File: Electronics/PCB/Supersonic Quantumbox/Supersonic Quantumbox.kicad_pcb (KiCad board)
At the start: 2 copper layers, 15 parts, among them J1 USB_C_Receptacle_USB2.0, U1 Input_jack, U2 TL071, U3 PCM1808PWR, U4 AZ1117-5.0, U5 ESP32-S2-WROVER-I, U6 AZ1117-3.3, U7 PCM5100, U8 Output_jack

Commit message: Start work on PCB
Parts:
- added C1: 100n, Capacitor_SMD:C_0805_2012Metric_Pad1.18x1.45mm_HandSolder, F.Cu at (132.0, 146.0)
- added C10: 10uF, Capacitor_SMD:C_1206_3216Metric, F.Cu at (257.1, 70.5)
- added C11: 100n, Capacitor_SMD:C_0805_2012Metric_Pad1.18x1.45mm_HandSolder, F.Cu at (265.0, 131.0)
- added C12: 100n, Capacitor_SMD:C_0805_2012Metric_Pad1.18x1.45mm_HandSolder, F.Cu at (176.0, 71.0)
- added C13: 100n, Capacitor_SMD:C_0805_2012Metric_Pad1.18x1.45mm_HandSolder, F.Cu at (146.0, 59.0)
- added C14: 100n, Capacitor_SMD:C_0805_2012Metric_Pad1.18x1.45mm_HandSolder, F.Cu at (250.9, 131.0)
- added C15: 2.2uF, Capacitor_SMD:C_1206_3216Metric, F.Cu at (246.0, 139.0)
- added C16: 2.2uF, Capacitor_SMD:C_1206_3216Metric, F.Cu at (248.0, 144.0)
- added C17: 100n, Capacitor_SMD:C_0805_2012Metric_Pad1.18x1.45mm_HandSolder, F.Cu at (257.9, 131.0)
- added C18: 10uF, Capacitor_SMD:C_1206_3216Metric, F.Cu at (266.0, 141.0)
- added C19: 2.2n, Capacitor_SMD:C_0805_2012Metric_Pad1.18x1.45mm_HandSolder, F.Cu at (257.0, 154.0)
- added C2: 10uF, Capacitor_SMD:C_1206_3216Metric, F.Cu at (124.0, 142.0)
- added C20: 100n, Capacitor_SMD:C_0805_2012Metric_Pad1.18x1.45mm_HandSolder, F.Cu at (141.0, 131.0)
- added C21: 10uF, Capacitor_SMD:C_1206_3216Metric, F.Cu at (191.0, 150.0)
- added C3: 10uF, Capacitor_SMD:C_1206_3216Metric, F.Cu at (144.0, 140.0)
- added C4: 100n, Capacitor_SMD:C_0805_2012Metric_Pad1.18x1.45mm_HandSolder, F.Cu at (187.0, 146.0)
- added C5: 100n, Capacitor_SMD:C_0805_2012Metric_Pad1.18x1.45mm_HandSolder, F.Cu at (199.0, 142.0)
- added C6: 100n, Capacitor_SMD:C_0805_2012Metric_Pad1.18x1.45mm_HandSolder, F.Cu at (195.0, 147.0)
- added C7: 10uF, Capacitor_SMD:C_1206_3216Metric, F.Cu at (221.8, 69.0)
- added C8: 10uF, Capacitor_SMD:C_1206_3216Metric, F.Cu at (257.1, 51.5)
- added C9: 10uF, Capacitor_SMD:C_1206_3216Metric, F.Cu at (222.3, 50.0)
- added J2: Barrel_Jack_Switch, Connector_BarrelJack:BarrelJack_Horizontal, F.Cu at (204.0, 99.0)
- added O1: 128x64_OLED, SupersonicQuantumbox:128x64OLED, F.Cu at (70.0, 94.0)
- added R1: 2M2, Resistor_SMD:R_0805_2012Metric_Pad1.20x1.40mm_HandSolder, F.Cu at (137.0, 146.0)
- added R10: 470, Resistor_SMD:R_0805_2012Metric_Pad1.20x1.40mm_HandSolder, F.Cu at (255.0, 148.0)
- added R11: 5.1K, Resistor_SMD:R_0805_2012Metric_Pad1.20x1.40mm_HandSolder, F.Cu at (255.0, 107.0)
- added R12: 5.1K, Resistor_SMD:R_0805_2012Metric_Pad1.20x1.40mm_HandSolder, F.Cu at (248.0, 106.0)
- added R2: 2M2, Resistor_SMD:R_0805_2012Metric_Pad1.20x1.40mm_HandSolder, F.Cu at (142.0, 146.0)
- added R3: 100K, Resistor_SMD:R_0805_2012Metric_Pad1.20x1.40mm_HandSolder, F.Cu at (127.0, 137.0)
- added R4: 220K, Resistor_SMD:R_0805_2012Metric_Pad1.20x1.40mm_HandSolder, F.Cu at (135.0, 129.0)
- added R5: 10K, Resistor_SMD:R_0805_2012Metric_Pad1.20x1.40mm_HandSolder, F.Cu at (179.0, 142.0)
- added R6: 10K, Resistor_SMD:R_0805_2012Metric_Pad1.20x1.40mm_HandSolder, F.Cu at (179.0, 138.0)
- added R7: 10K, Resistor_SMD:R_0805_2012Metric_Pad1.20x1.40mm_HandSolder, F.Cu at (175.0, 140.0)
- added R8: 10K, Resistor_SMD:R_0805_2012Metric_Pad1.20x1.40mm_HandSolder, F.Cu at (177.0, 65.0)
- added R9: 470, Resistor_SMD:R_0805_2012Metric_Pad1.20x1.40mm_HandSolder, F.Cu at (250.0, 151.0)
- added SW1: RESET, Button_Switch_SMD:SW_Push_1P1T_NO_6x6mm_H9.5mm, F.Cu at (186.0, 68.0)
- added SW2: BOOT, Button_Switch_SMD:SW_Push_1P1T_NO_6x6mm_H9.5mm, F.Cu at (133.0, 70.0)
- U1, U8: moved to B.Cu
- moved J1 117.9 mm to (251.0, 95.0), turned to 90 degrees
- moved RV4 111.6 mm to (46.0, 66.8), turned to -90 degrees
- moved U1 103.9 mm to (54.0, 123.5)
- moved RV1 101.9 mm to (46.0, 43.8), turned to -90 degrees
- moved RV3 98.3 mm to (94.0, 43.8), turned to -90 degrees
- moved RV5 97.9 mm to (70.0, 66.8), turned to -90 degrees
- moved RV2 95.7 mm to (70.0, 43.8), turned to -90 degrees
- moved U7 91.4 mm to (258.0, 139.0)
- moved U4 87.3 mm to (256.6, 60.5)
- moved U6 81.9 mm to (222.8, 60.0)
- moved U3 73.1 mm to (189.0, 139.0), turned to 180 degrees
- moved U5 65.6 mm to (159.0, 68.0)
- moved RV6 60.3 mm to (94.0, 66.8), turned to -90 degrees
- moved U2 11.8 mm to (136.0, 137.0)
- moved U8 11.2 mm to (86.0, 123.5), turned to 180 degrees
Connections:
- J1 pad A5: unconnected-(J1-PadA5) -> Net-(J1-PadA5)
- J1 pad B5: unconnected-(J1-PadB5) -> Net-(J1-PadB5)
- RV1 pad 2: unconnected-(RV1-Pad2) -> /Pot1
- RV2 pad 2: unconnected-(RV2-Pad2) -> /Pot2
- RV3 pad 2: unconnected-(RV3-Pad2) -> /Pot3
- RV4 pad 2: unconnected-(RV4-Pad2) -> /Pot4
- RV5 pad 2: unconnected-(RV5-Pad2) -> /Pot5
- RV6 pad 2: unconnected-(RV6-Pad2) -> /Pot6
- U5 pad 10: /LRCK -> unconnected-(U5-Pad10)
- U5 pad 14: unconnected-(U5-Pad14) -> /SDA
- U5 pad 15: unconnected-(U5-Pad15) -> /SCL
- U5 pad 16: unconnected-(U5-Pad16) -> /BCK
- U5 pad 17: unconnected-(U5-Pad17) -> /LRCK
- U5 pad 20: unconnected-(U5-Pad20) -> Net-(U3-Pad9)
- U5 pad 21: Net-(U3-Pad9) -> /DIN
- U5 pad 22: unconnected-(U5-Pad22) -> /USB_D-
- U5 pad 23: unconnected-(U5-Pad23) -> /USB_D+
- U5 pad 4: unconnected-(U5-Pad4) -> /Pot1
- U5 pad 41: unconnected-(U5-Pad41) -> /EN
- U5 pad 5: unconnected-(U5-Pad5) -> /Pot2
- U5 pad 6: unconnected-(U5-Pad6) -> /Pot3
- U5 pad 7: /BCK -> /Pot4
- U5 pad 8: unconnected-(U5-Pad8) -> /Pot5
- U5 pad 9: unconnected-(U5-Pad9) -> /Pot6
- U7 pad 1: unconnected-(U7-Pad1) -> +3V3
- U7 pad 12: unconnected-(U7-Pad12) -> GNDREF
- U7 pad 14: unconnected-(U7-Pad14) -> /DIN
- U7 pad 18: unconnected-(U7-Pad18) -> Net-(C17-Pad1)
- U7 pad 2: unconnected-(U7-Pad2) -> Net-(C15-Pad1)
- U7 pad 20: unconnected-(U7-Pad20) -> +3V3
- U7 pad 4: unconnected-(U7-Pad4) -> Net-(C15-Pad2)
- U7 pad 5: unconnected-(U7-Pad5) -> Net-(C16-Pad1)
- U7 pad 6: unconnected-(U7-Pad6) -> Net-(R9-Pad1)
- U7 pad 7: unconnected-(U7-Pad7) -> Net-(R10-Pad1)
- U7 pad 8: unconnected-(U7-Pad8) -> +3V3
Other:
- board outline added: 70 x 100 mm

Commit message: POT and screen adjustment
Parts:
- O1: moved to B.Cu
- moved O1 32.0 mm to (70.0, 62.0), turned to 180 degrees
- moved RV5 12.3 mm to (70.0, 79.2), turned to 90 degrees
- moved RV4 6.43 mm to (47.0, 73.2), turned to 30 degrees
- moved RV6 6.41 mm to (93.0, 73.2), turned to 150 degrees
- moved RV2 3.66 mm to (70.0, 40.2)
- moved RV3 3.47 mm to (93.0, 47.2), turned to -150 degrees
- moved RV1 3.16 mm to (47.0, 46.8), turned to -30 degrees

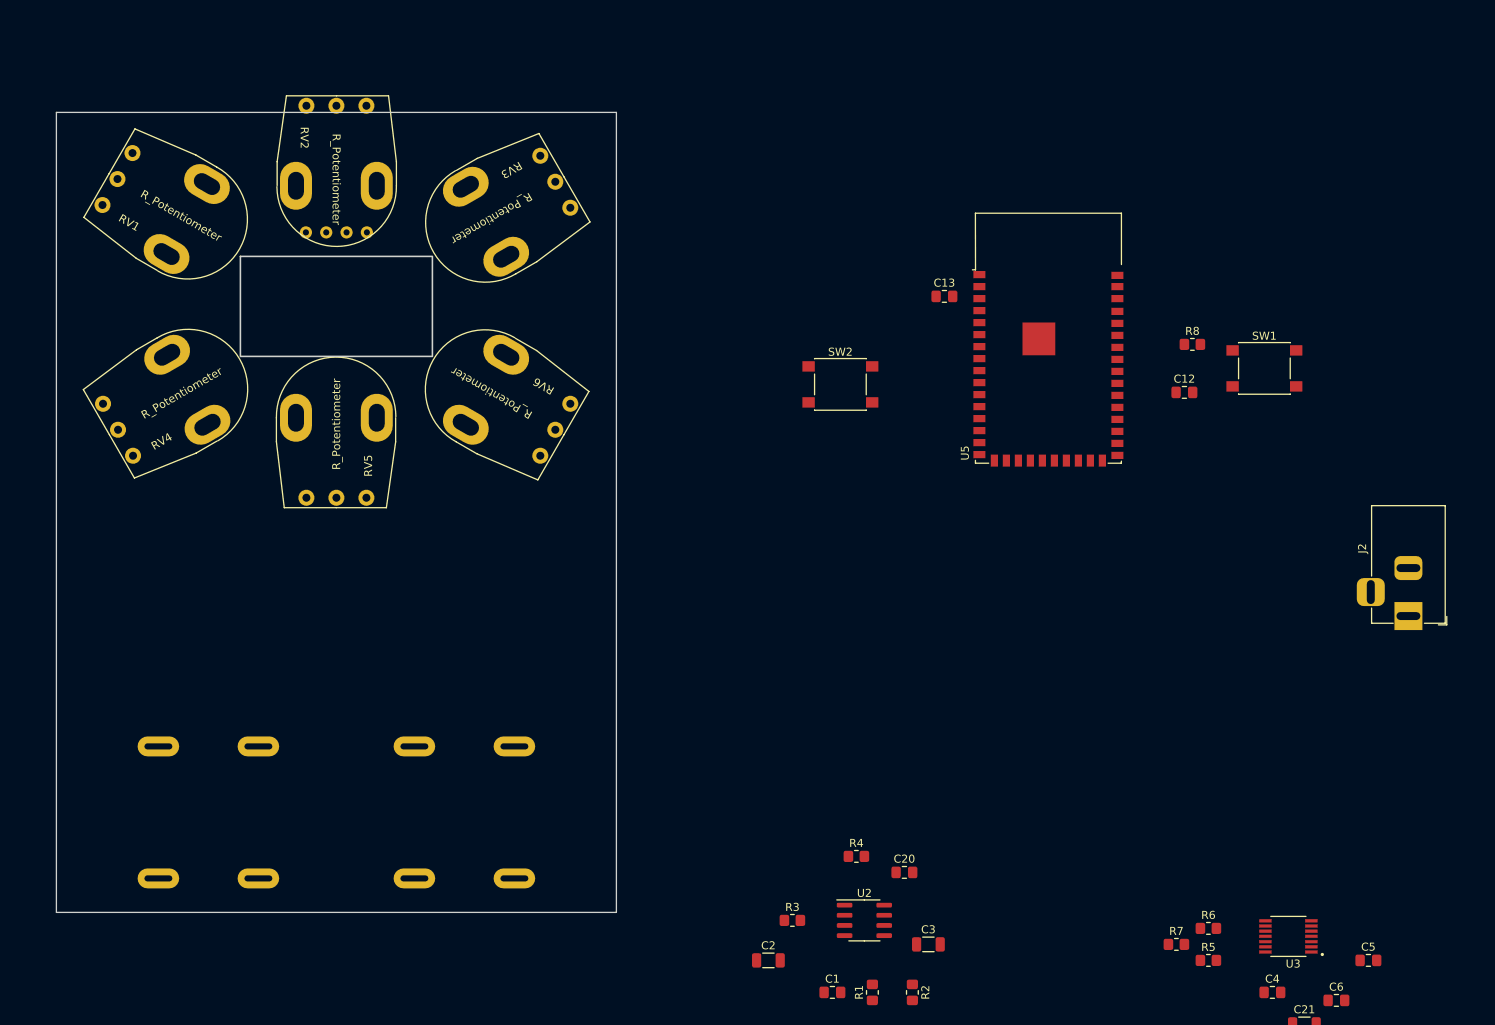
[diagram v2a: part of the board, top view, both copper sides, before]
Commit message: Change PCB layout
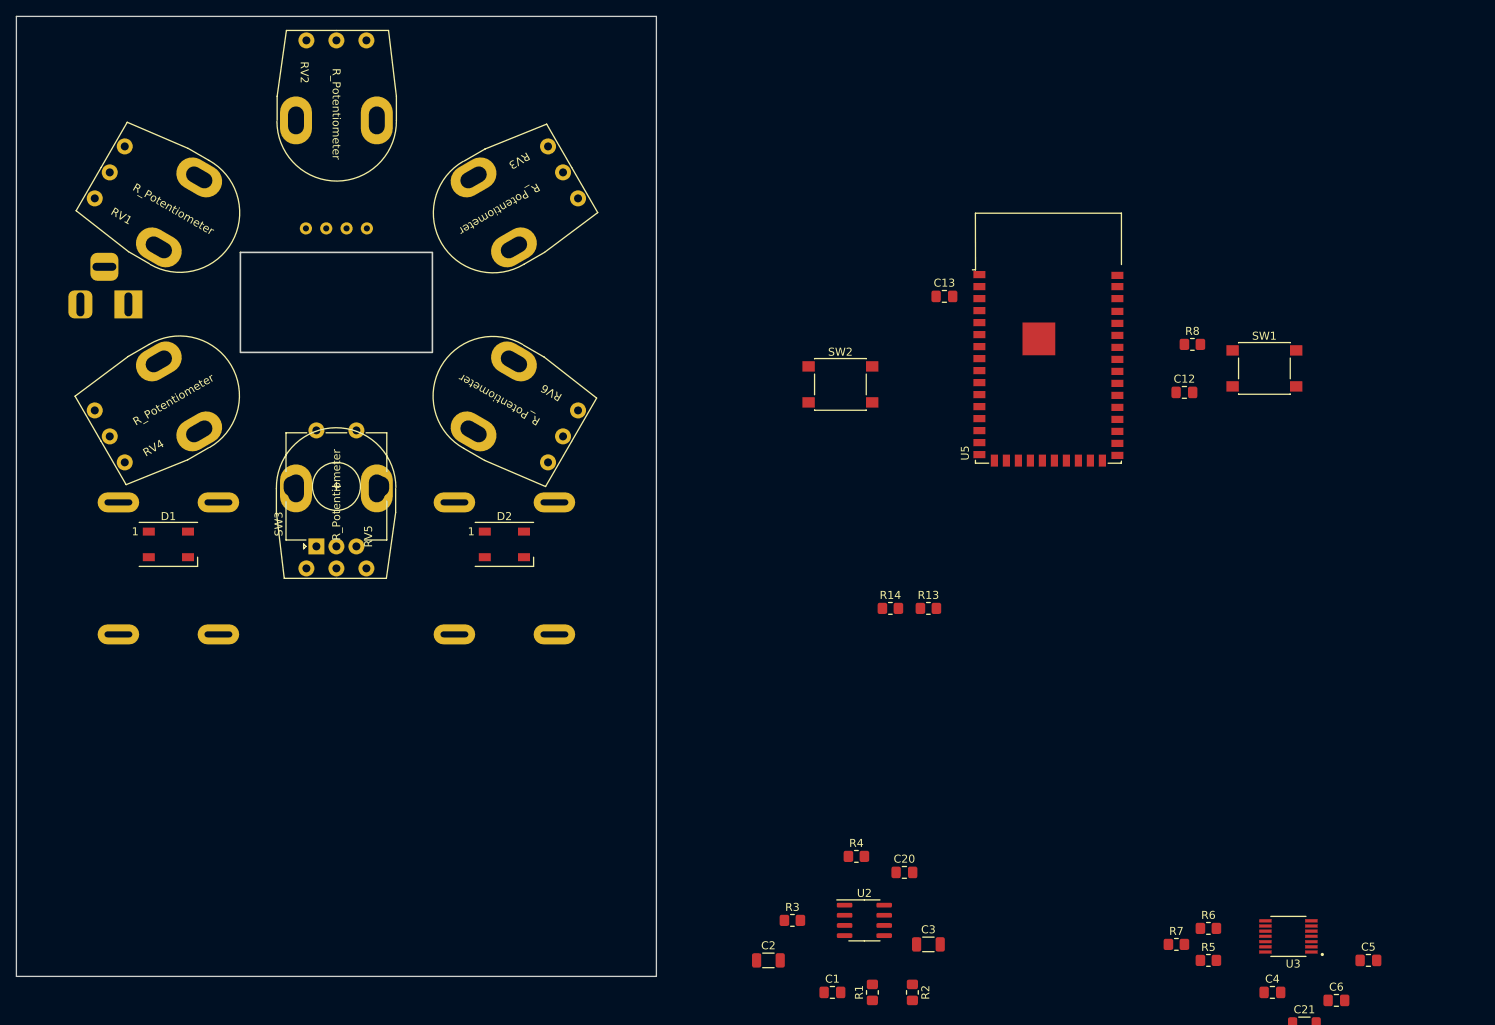
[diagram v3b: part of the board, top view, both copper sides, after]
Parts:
- added D1: WS2812B, LED_SMD:LED_WS2812B_PLCC4_5.0x5.0mm_P3.2mm, F.Cu at (49.0, 90.0)
- added D2: WS2812B, LED_SMD:LED_WS2812B_PLCC4_5.0x5.0mm_P3.2mm, F.Cu at (91.0, 90.0)
- added R13: 10K, Resistor_SMD:R_0805_2012Metric_Pad1.20x1.40mm_HandSolder, F.Cu at (144.0, 98.0)
- added R14: 10K, Resistor_SMD:R_0805_2012Metric_Pad1.20x1.40mm_HandSolder, F.Cu at (139.2, 98.0)
- added SW3: RotaryEncoder_Switch, Rotary_Encoder:RotaryEncoder_Alps_EC12E-Switch_Vertical_H20mm, F.Cu at (67.5, 90.2)
- J2: moved to B.Cu
- moved J2 164.7 mm to (44.0, 60.0), turned to 0 degrees
- moved U1 30.9 mm to (49.0, 93.0)
- moved U8 30.9 mm to (91.0, 93.0)
- moved RV5 8.83 mm to (70.0, 88.0)
- moved RV2 8.17 mm to (70.0, 32.0)
- moved O1 2.00 mm to (70.0, 60.0)
- moved RV3 1.52 mm to (94.0, 46.0)
- moved RV4 1.33 mm to (46.0, 74.0)
- moved RV6 1.27 mm to (94.0, 74.0)
- moved RV1 1.27 mm to (46.0, 46.0)
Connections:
- U5 pad 10: unconnected-(U5-Pad10) -> /ENC_SW
- U5 pad 11: unconnected-(U5-Pad11) -> /ENC_B
- U5 pad 12: unconnected-(U5-Pad12) -> /ENC_A
- U5 pad 13: unconnected-(U5-Pad13) -> /NEOP
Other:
- board size 70 x 100 mm -> 80 x 120 mm

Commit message: Routing
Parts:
- added C22: 100n, Capacitor_SMD:C_0805_2012Metric_Pad1.18x1.45mm_HandSolder, B.Cu at (165.5, 65.5)
- added C23: 100n, Capacitor_SMD:C_0805_2012Metric_Pad1.18x1.45mm_HandSolder, B.Cu at (200.5, 65.5)
- added D5: PWR_LED, LED_SMD:LED_0805_2012Metric_Pad1.15x1.40mm_HandSolder, B.Cu at (209.0, 91.0)
- added H1: M3, MountingHole:MountingHole_3.2mm_M3_Pad_Via, F.Cu at (147.0, 163.5)
- added H2: M3, MountingHole:MountingHole_3.2mm_M3_Pad_Via, F.Cu at (219.0, 163.5)
- added H3: M3, MountingHole:MountingHole_3.2mm_M3_Pad_Via, F.Cu at (147.0, 21.5)
- added H4: M3, MountingHole:MountingHole_3.2mm_M3_Pad_Via, F.Cu at (219.0, 21.5)
- added J3: UART, Connector_PinHeader_2.54mm:PinHeader_1x02_P2.54mm_Vertical, F.Cu at (181.7, 135.8)
- added J4: GPIO2, Connector_PinSocket_2.54mm:PinSocket_1x05_P2.54mm_Vertical, F.Cu at (181.7, 133.1)
- added J5: GPIO1, Connector_PinSocket_2.54mm:PinSocket_1x05_P2.54mm_Vertical, F.Cu at (184.3, 122.9)
- added JP1: GND_JMP, Jumper:SolderJumper-2_P1.3mm_Open_TrianglePad1.0x1.5mm, B.Cu at (145.0, 157.7)
- added R15: R_LED, Resistor_SMD:R_0805_2012Metric_Pad1.20x1.40mm_HandSolder, B.Cu at (209.0, 95.0)
- added SW4: SW_DPDT_x2, SupersonicQuantumbox:Stomp_switch, F.Cu at (183.0, 151.0)
- C1, C10, C11, C12, C13, C14, C15, C16, C17, C18, C19, C2, C20, C21, C3, C4, C5, C6, C7, C8, C9, J1, R1, R10, R11, R12, R13, R14, R2, R3, R4, R6, R8, R9, SW1, SW2, U2, U3, U4, U5, U6, U7: moved to B.Cu
- R5, R7: value 10K -> R_LED; moved to B.Cu
- U1, U8: footprint GustavsGlobalLibrary:Mono jack SYS212 -> SupersonicQuantumbox:MonoJack-SYS212
- moved U1 159.5 mm to (204.0, 130.5), turned to 180 degrees
- moved D1 122.4 mm to (167.5, 59.5), turned to -90 degrees
- moved SW3 118.1 mm to (185.5, 85.0), turned to -90 degrees
- moved J2 113.0 mm to (157.0, 59.5)
- moved O1 113.0 mm to (183.0, 59.5)
- moved RV1 113.0 mm to (159.0, 45.5), turned to 150 degrees
- moved RV3 113.0 mm to (207.0, 45.5), turned to 30 degrees
- moved RV4 113.0 mm to (159.0, 73.5), turned to -150 degrees
- moved RV5 113.0 mm to (183.0, 87.5), turned to -90 degrees
- moved RV6 113.0 mm to (207.0, 73.5), turned to -30 degrees
- moved RV2 113.0 mm to (183.0, 31.7), turned to 90 degrees
- moved D2 111.7 mm to (198.5, 59.5), turned to 90 degrees
- moved C11 110.3 mm to (155.5, 144.0), turned to 90 degrees
- moved C10 102.3 mm to (166.5, 23.0)
- moved C18 101.0 mm to (165.0, 143.0), turned to 90 degrees
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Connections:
- net Net-(C19-Pad1) renamed /DSP_OUT
- C1 pad 1: /Input_signal -> /DSP_IN
- D1 pad 1: +5V -> +3V3
- D2 pad 1: +5V -> +3V3
- R5 pad 1: GNDREF -> /LED2
- R7 pad 1: GNDREF -> /LED1
- U1 pad 1: /Input_signal -> /JACK_IN
- U3 pad 11: Net-(R7-Pad2) -> Net-(R6-Pad2)
- U3 pad 12: Net-(R5-Pad2) -> Net-(R6-Pad2)
- U3 pad 9: Net-(U3-Pad9) -> /DOUT
- U5 pad 10: /ENC_SW -> /SDA
- U5 pad 11: /ENC_B -> /Pot6
- U5 pad 12: /ENC_A -> /Pot5
- U5 pad 13: /NEOP -> /ENC_B
- U5 pad 14: /SDA -> /ENC_A
- U5 pad 15: /SCL -> /ENC_SW
- U5 pad 16: /BCK -> /LED1
- U5 pad 17: /LRCK -> /LED2
- U5 pad 18: unconnected-(U5-Pad18) -> /BCK
- U5 pad 19: unconnected-(U5-Pad19) -> /DOUT
- U5 pad 20: Net-(U3-Pad9) -> /DIN
- U5 pad 21: /DIN -> /LRCK
- U5 pad 27: unconnected-(U5-Pad27) -> /IO33
- U5 pad 28: unconnected-(U5-Pad28) -> /IO34
- U5 pad 29: unconnected-(U5-Pad29) -> /IO35
- U5 pad 30: unconnected-(U5-Pad30) -> /IO36
- U5 pad 31: unconnected-(U5-Pad31) -> /IO37
- U5 pad 32: unconnected-(U5-Pad32) -> /IO38
- U5 pad 33: unconnected-(U5-Pad33) -> /IO39
- U5 pad 34: unconnected-(U5-Pad34) -> /IO40
- U5 pad 37: unconnected-(U5-Pad37) -> /TX
- U5 pad 38: unconnected-(U5-Pad38) -> /RX
- U5 pad 8: /Pot5 -> /NEOP
- U5 pad 9: /Pot6 -> /SCL
- U8 pad 1: /Output_signal -> /JACK_OUT
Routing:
- net /EN: track 0.00 -> 113.7 mm, vias 0 -> 4
- net /BCK: track 0.00 -> 90.1 mm, vias 0 -> 2
- net /Pot3: track 0.00 -> 85.2 mm
- net /IO0: track 0.00 -> 83.6 mm, vias 0 -> 2
- net /LRCK: track 0.00 -> 81.7 mm, vias 0 -> 2
- net /SCL: track 0.00 -> 78.7 mm
- net /SDA: track 0.00 -> 76.3 mm
- net /Pot2: track 0.00 -> 74.2 mm
- net /DIN: track 0.00 -> 55.5 mm, vias 0 -> 2
- net /Pot1: track 0.00 -> 54.5 mm
- net /Pot6: track 0.00 -> 54.0 mm
- net /USB_D+: track 0.00 -> 46.1 mm, vias 0 -> 2
- net /USB_D-: track 0.00 -> 46.0 mm, vias 0 -> 2
- net Net-(D1-Pad2): track 0.00 -> 44.4 mm, vias 0 -> 2
- net /NEOP: track 0.00 -> 38.5 mm, vias 0 -> 1
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- added copper zone on F.Cu, net GNDREF
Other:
- board size 80 x 120 mm -> 80 x 150 mm
- board text added: "3.3V"
- board text added: "BND"
- board text added: "IO33"
- board text added: "IO34"
- board text added: "IO35"
- board text added: "IO36"
- board text added: "IO37"
- board text added: "IO38"
- board text added: "IO39"
- board text added: "IO40"
- board text added: "RX"
- board text added: "TX"

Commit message: Begin PWR tracing
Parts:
- added D3: LED2, SupersonicQuantumbox:38 mm LED, F.Cu at (146.0, 59.5)
- added D4: LED1, SupersonicQuantumbox:38 mm LED, F.Cu at (220.0, 59.5)
- moved C2 3.32 mm to (219.5, 143.5), turned to 180 degrees
- moved C18 3.16 mm to (162.0, 144.0), turned to 0 degrees
- moved R13 1.00 mm to (193.5, 84.5)
- moved R14 1.00 mm to (172.5, 84.5)
- moved R3 0.59 mm to (218.0, 147.1)
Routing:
- net +5V: track 7.52 -> 188.7 mm, vias 0 -> 2
- net +3V3: track 0.00 -> 140.9 mm, vias 0 -> 4
- net Net-(D3-Pad2): track 0.00 -> 99.6 mm, vias 0 -> 4
- net +9V: track 0.00 -> 95.2 mm
- net Net-(D4-Pad2): track 0.00 -> 48.3 mm
- net /LED1: track 0.46 -> 34.6 mm
- net /LED2: track 0.00 -> 32.8 mm
- net /BCK: track 90.1 -> 91.3 mm
- net /DOUT: track 32.2 -> 33.4 mm
- net Net-(D1-Pad2): track 44.4 -> 45.5 mm
- net Net-(C17-Pad1): track 12.9 -> 11.9 mm
- net Net-(R3-Pad2): track 13.2 -> 12.2 mm
- net /ENC_A: track 28.5 -> 29.5 mm
- net Net-(C2-Pad2): track 3.53 -> 2.61 mm
- net /LRCK: track 81.7 -> 81.1 mm
- added copper zone on B.Cu, net GNDREF

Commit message: Final routing
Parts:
- moved C10 33.8 mm to (197.5, 36.5)
- moved C7 29.0 mm to (168.0, 23.0)
- moved C9 14.0 mm to (197.5, 23.0)
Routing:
- net +3V3: track 140.9 -> 379.6 mm, vias 4 -> 9
- net +9V: track 95.2 -> 256.2 mm
- net GNDREF: track 0.00 -> 93.9 mm, vias 0 -> 204
- net /LED1: track 34.6 -> 39.0 mm
- net +5V: track 188.7 -> 185.1 mm
- net /IO0: track 83.6 -> 87.1 mm
- net /TX: track 36.9 -> 38.8 mm
- net /LED2: track 32.8 -> 34.5 mm
- net Net-(C17-Pad1): track 11.9 -> 10.7 mm
- net /Pot5: track 30.9 -> 30.4 mm
- net Net-(C15-Pad1): track 15.5 -> 15.0 mm
- net (no net): vias 0 -> 1

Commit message: Almost finish PCB
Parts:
- added G***: LOGO, LOGO, F.Cu at (207.0, 154.5)
- added G***: LOGO, LOGO, F.Cu at (154.5, 163.5)
- added REF**: KiCad-Logo2_5mm_SilkScreen, Symbol:KiCad-Logo2_5mm_SilkScreen, F.Cu at (207.0, 163.0)
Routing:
- net GNDREF: vias 204 -> 212
- net (no net): vias 1 -> 0
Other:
- board text added: "2022 v1.0"
- board text added: "A. Anderson G. Abrahamsson"
- board text added: "Supersonic Quantumbox"

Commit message: Final touches
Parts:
- added G***: LOGO, LOGO, F.Cu at (212.0, 163.5)
- C19: value 2.2n -> 22n
- R10, R9: value 470 -> 470R
- moved G*** 141.7 mm to (155.5, 22.5)
- moved REF** 141.5 mm to (208.0, 21.5)
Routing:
- net GNDREF: vias 212 -> 227
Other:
- board text added: "+9V"
- board text added: "3V3"
- board text added: "A. Anderson"
- board text added: "G. Abrahamsson"
- board text added: "GND"
- board text added: "IN"
- board text added: "JLCJLCJLCJLC"
- board text added: "OUT"
- board text added: "Pot1"
- board text added: "Pot2"
- board text added: "Pot3"
- board text added: "Pot4"
- board text added: "Pot5"
- board text added: "Pot6"
- board text added: "SCL"
- board text added: "SDA"
- board text removed: "A. Anderson G. Abrahamsson"
